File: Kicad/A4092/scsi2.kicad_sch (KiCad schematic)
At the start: 33 parts, among them U9 LSI53C770 SCSI Host Controller

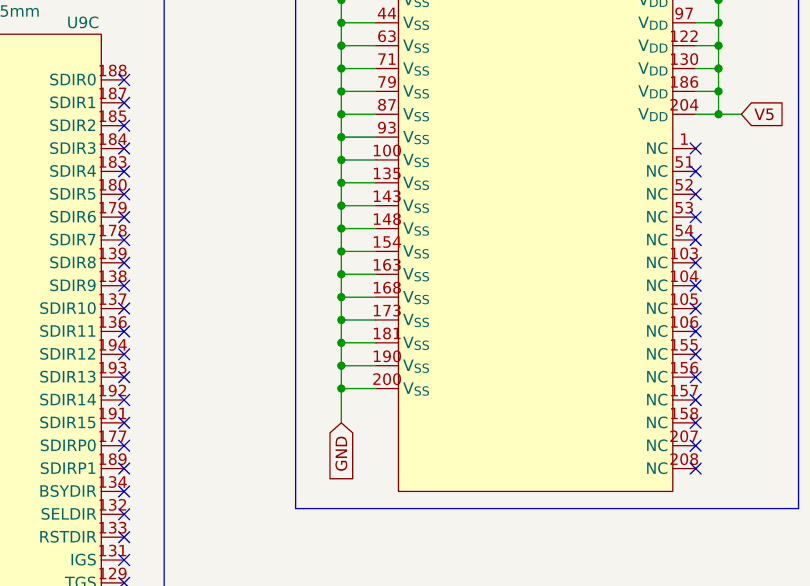
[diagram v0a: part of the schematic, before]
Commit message: Fix NCR53C770 footprint
P119 (Vss) was not in correctly assigned in the footprint.
Added it, and connected to Vss.
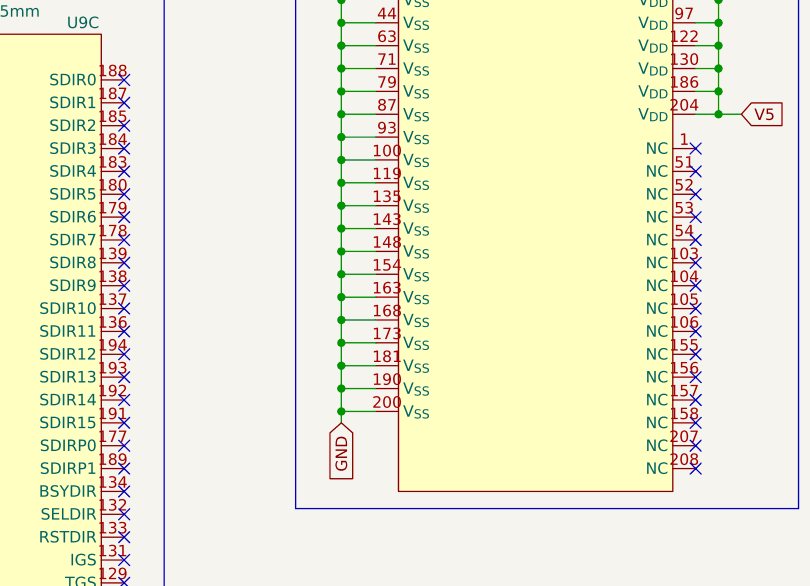
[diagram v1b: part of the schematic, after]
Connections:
- net GND: now also U9.119 (V_{SS})
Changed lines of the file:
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@@
 	)
 	(junction
+		(at 191.77 153.67)
+		(diameter 0)
+		(color 0 0 0 0)
+	)
+	(junction
 		(at 260.35 48.26)
 		(diameter 0)
@@
 	(wire
 		(pts
-			(xy 191.77 151.13) (xy 191.77 154.94)
+			(xy 191.77 151.13) (xy 191.77 153.67)
 		)
 		(stroke
@@
 	(wire
 		(pts
+			(xy 191.77 153.67) (xy 195.58 153.67)
+		)
+		(stroke
+			(width 0)
+			(type default)
+		)
+	)
+	(wire
+		(pts
 			(xy 269.24 24.13) (xy 271.78 24.13)
 		)
@@
 	(wire
 		(pts
+			(xy 191.77 153.67) (xy 191.77 154.94)
+		)
+		(stroke
+			(width 0)
+			(type default)
+		)
+	)
+	(wire
+		(pts
 			(xy 273.05 59.69) (xy 273.05 55.88)
 		)
@@
 	)
 	(symbol
+		(lib_name "LSI53C770_2")
 		(lib_id "NCRSCSI:LSI53C770")
 		(at 213.36 128.27 0)
@@
 		(pin "107"
 		)
+		(pin "119"
+		)
 		(instances

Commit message: Clean up pull-up resistors
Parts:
- removed R100, R101, R102, R103, R94, R95: 1K, Resistor_SMD:R_0603_1608Metric_Pad0.98x0.95mm_HandSolder, symbol Device:R_Small
- R96, R99: now not fitted
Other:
- title: A4092 -> Cheetah UW
- moved on the sheet: R104, R105, R106, R107, R90, R91, R92, R93, R97, R98

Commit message: Rehaul clock circuit in schematics
and try to add most of the LCSC part numbers
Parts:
- R104, R105, R106, R107, R90, R91, R92, R93, R96, R97, R98, R99: LCSC Part # (none) -> C21190
- R108, R109, R110, R111, R112: LCSC Part # (none) -> C25804
- U9: LCSC Part # (none) -> C9900193416
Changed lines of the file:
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@@
 			)
 		)
+		(property "LCSC Part #" "C21190"
+			(at 265.43 26.67 90)
+			(effects
+				(font
+					(size 1.27 1.27)
+				)
+				(hide yes)
+			)
+		)
 		(pin "2"
 		)
@@
 			)
 		)
+		(property "LCSC Part #" "C9900193416"
+			(at 213.36 128.27 0)
+			(effects
+				(font
+					(size 1.27 1.27)
+				)
+				(hide yes)
+			)
+		)
 		(pin "29"
 		)
@@
 			)
 		)
+		(property "LCSC Part #" "C9900193416"
+			(at 134.62 59.69 0)
+			(effects
+				(font
+					(size 1.27 1.27)
+				)
+				(hide yes)
+			)
+		)
 		(pin "29"
 		)
@@
 			)
 		)
+		(property "LCSC Part #" "C21190"
+			(at 273.05 26.67 90)
+			(effects
+				(font
+					(size 1.27 1.27)
+				)
+				(hide yes)
+			)
+		)
 		(pin "2"
 		)
@@
 			)
 		)
+		(property "LCSC Part #" "C25804"
+			(at 166.37 95.25 90)
+			(effects
+				(font
+					(size 1.27 1.27)
+				)
+				(hide yes)
+			)
+		)
 		(pin "2"
 		)
@@
 			)
 		)
+		(property "LCSC Part #" "C21190"
+			(at 267.97 26.67 90)
+			(effects
+				(font
+					(size 1.27 1.27)
+				)
+				(hide yes)
+			)
+		)
 		(pin "2"
 		)
@@
 			)
 		)
+		(property "LCSC Part #" "C25804"
+			(at 166.37 92.71 90)
+			(effects
+				(font
+					(size 1.27 1.27)
+				)
+				(hide yes)
+			)
+		)
 		(pin "2"
 		)
@@
 			)
 		)
+		(property "LCSC Part #" "C9900193416"
+			(at 49.53 72.39 0)
+			(effects
+				(font
+					(size 1.27 1.27)
+				)
+				(hide yes)
+			)
+		)
 		(pin "29"
 		)
@@
 			)
 		)
+		(property "LCSC Part #" "C21190"
+			(at 280.67 26.67 90)
+			(effects
+				(font
+					(size 1.27 1.27)
+				)
+				(hide yes)
+			)
+		)
 		(pin "2"
 		)
@@
 			)
 		)
+		(property "LCSC Part #" "C21190"
+			(at 257.81 26.67 90)
+			(effects
+				(font
+					(size 1.27 1.27)
+				)
+				(hide yes)
+			)
+		)
 		(pin "2"
 		)
@@
 			)
 		)
+		(property "LCSC Part #" "C25804"
+			(at 166.37 87.63 90)
+			(effects
+				(font
+					(size 1.27 1.27)
+				)
+				(hide yes)
+			)
+		)
 		(pin "2"
 		)
@@
 			)
 		)
+		(property "LCSC Part #" "C25804"
+			(at 166.37 81.28 90)
+			(effects
+				(font
+					(size 1.27 1.27)
+				)
+				(hide yes)
+			)
+		)
 		(pin "2"
 		)
@@
 			)
 		)
+		(property "LCSC Part #" "C21190"
+			(at 278.13 26.67 90)
+			(effects
+				(font
+					(size 1.27 1.27)
+				)
+				(hide yes)
+			)
+		)
 		(pin "2"
 		)
@@
 			)
 		)
+		(property "LCSC Part #" "C21190"
+			(at 270.51 26.67 90)
+			(effects
+				(font
+					(size 1.27 1.27)
+				)
+				(hide yes)
+			)
+		)
 		(pin "2"
 		)
@@
 			)
 		)
+		(property "LCSC Part #" "C21190"
+			(at 260.35 26.67 90)
+			(effects
+				(font
+					(size 1.27 1.27)
+				)
+				(hide yes)
+			)
+		)
 		(pin "2"
 		)
@@
 			)
 		)
+		(property "LCSC Part #" "C21190"
+			(at 262.89 26.67 90)
+			(effects
+				(font
+					(size 1.27 1.27)
+				)
+				(hide yes)
+			)
+		)
 		(pin "2"
 		)
@@
 			)
 		)
+		(property "LCSC Part #" "C21190"
+			(at 275.59 26.67 90)
+			(effects
+				(font
+					(size 1.27 1.27)
+				)
+				(hide yes)
+			)
+		)
 		(pin "2"
 		)
@@
 			)
 		)
+		(property "LCSC Part #" "C21190"
+			(at 252.73 26.67 90)
+			(effects
+				(font
+					(size 1.27 1.27)
+				)
+				(hide yes)
+			)
+		)
 		(pin "2"
 		)
@@
 			)
 		)
+		(property "LCSC Part #" "C9900193416"
+			(at 138.43 152.4 0)
+			(effects
+				(font
+					(size 1.27 1.27)
+				)
+				(hide yes)
+			)
+		)
 		(pin "29"
 		)
@@
 			)
 		)
+		(property "LCSC Part #" "C25804"
+			(at 166.37 90.17 90)
+			(effects
+				(font
+					(size 1.27 1.27)
+				)
+				(hide yes)
+			)
+		)
 		(pin "2"
 		)
@@
 			(effects
 				(font
+					(size 1.27 1.27)
+				)
+				(hide yes)
+			)
+		)
+		(property "LCSC Part #" "C21190"
+			(at 255.27 26.67 90)
+			(effects
+				(font
